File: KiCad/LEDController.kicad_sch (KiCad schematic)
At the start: 59 parts, among them J1 UART, J2 VDD, J3 GND, J4 Conn_01x05, J5 Conn_01x03, J6 USB_C_Receptacle_USB2.0_16P, J7 Conn_01x14, J8 JTAG, Q1 IRLZ44N, Q2 IRLZ44N, Q3 IRLZ44N, Q4 IRLZ44N, SW1 BOOT, SW2 EN, U1 TPS54202DDC, U2 ESP32-S3-WROOM-2, U3 TPS54202DDC

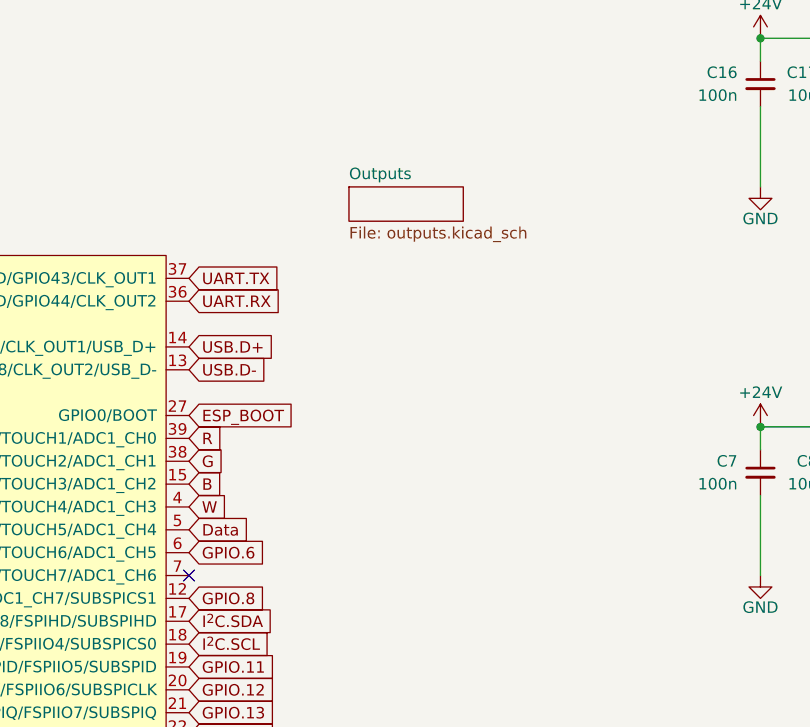
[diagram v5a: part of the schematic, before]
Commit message: add relay
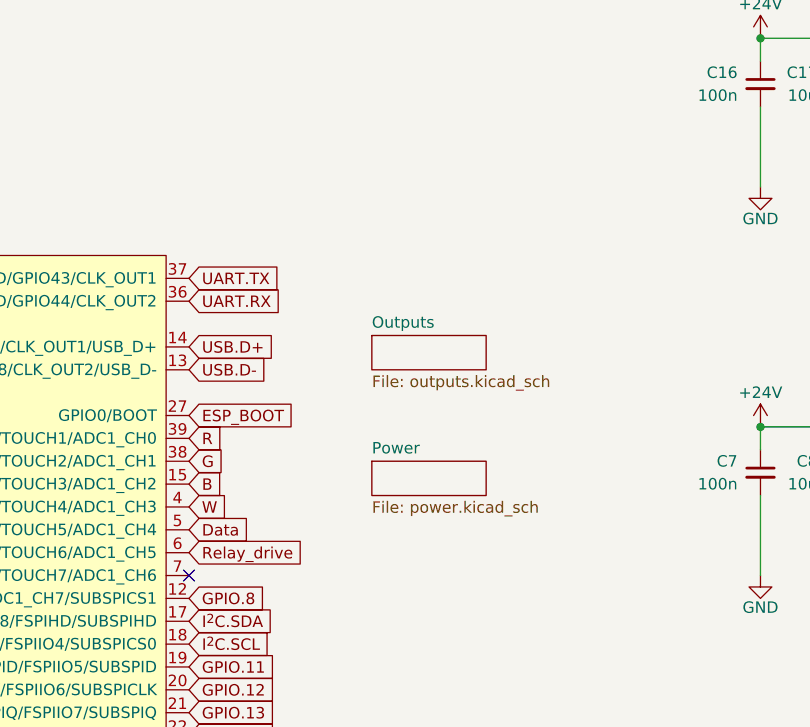
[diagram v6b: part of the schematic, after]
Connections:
- net GPIO.6: no longer U2.6 (GPIO6/TOUCH6/ADC1_CH5)
- new net Relay_drive: U2.6 (GPIO6/TOUCH6/ADC1_CH5)
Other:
- added sheet Power (power.kicad_sch)

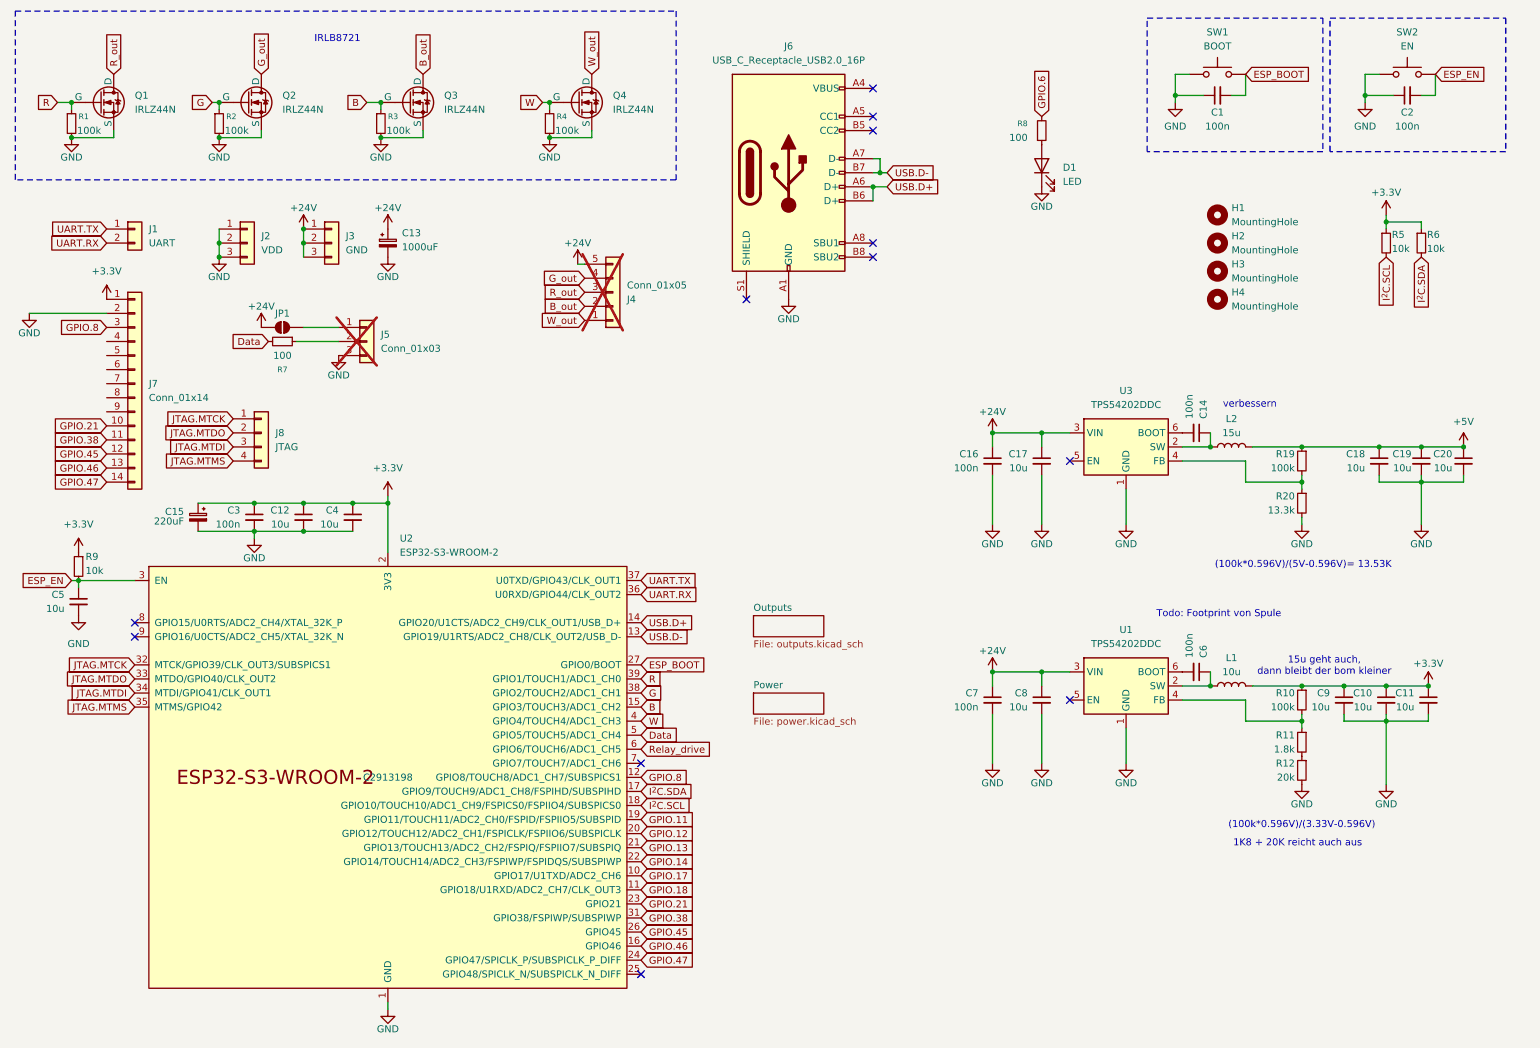
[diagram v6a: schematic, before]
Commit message: delete pwm, add 12 neopixel outputs
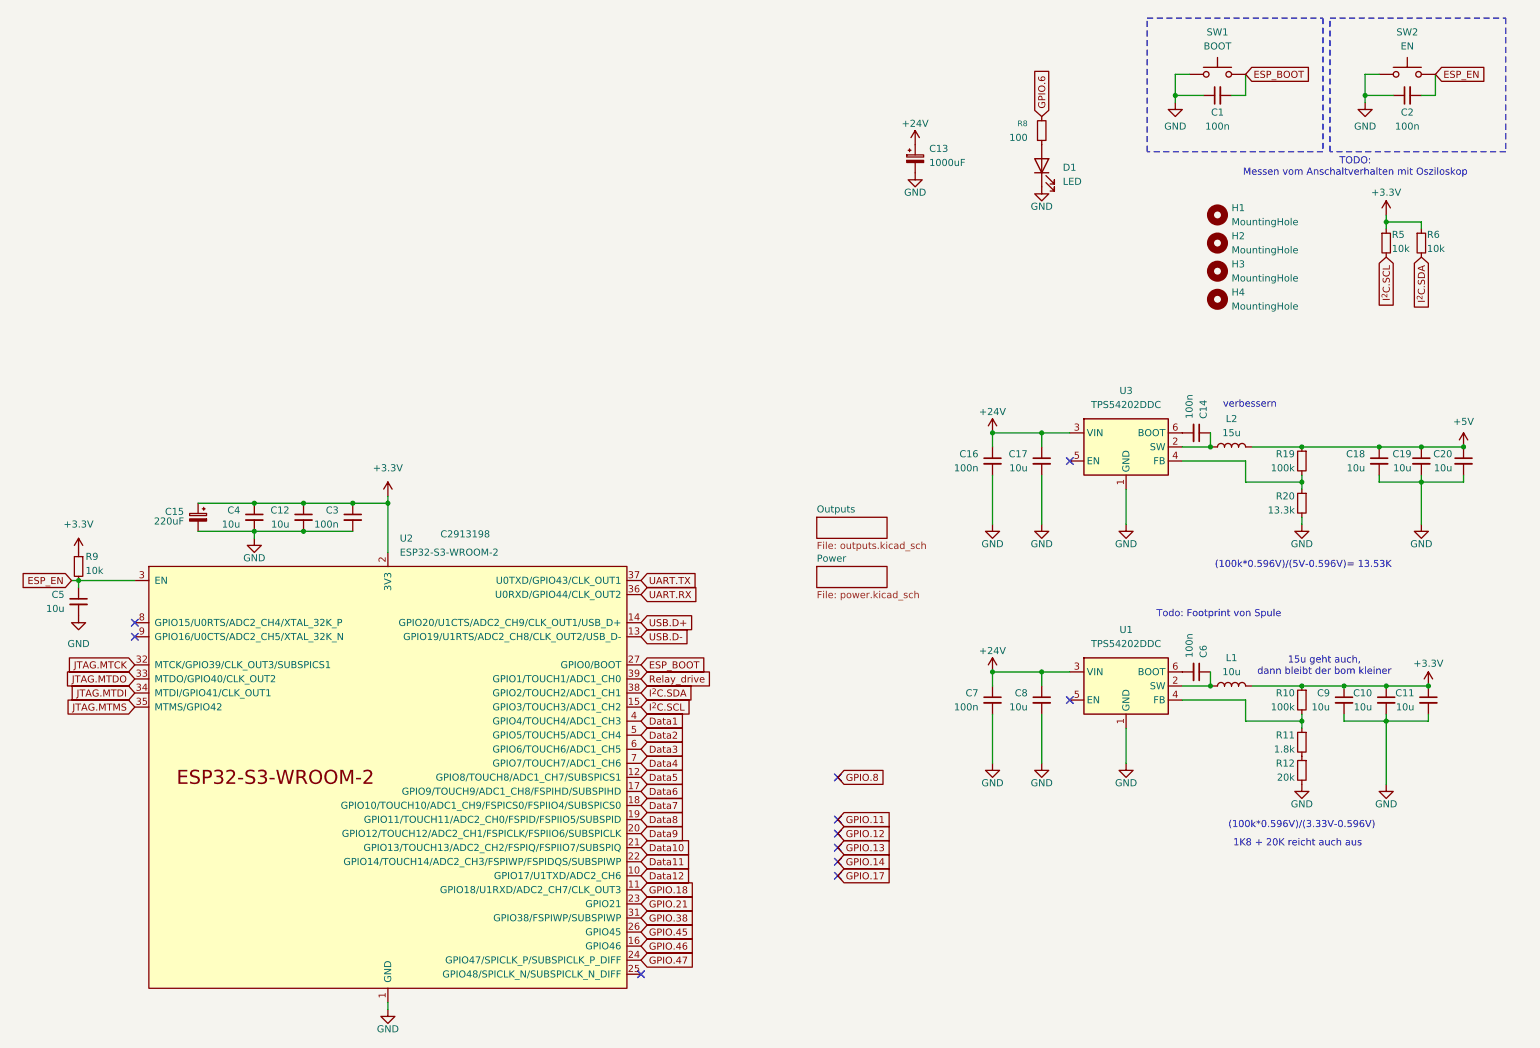
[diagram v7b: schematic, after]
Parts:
- removed J1: UART, Connector_PinHeader_2.54mm:PinHeader_1x02_P2.54mm_Vertical, symbol Connector_Generic:Conn_01x02
- removed J2: VDD, TerminalBlock_Phoenix:TerminalBlock_Phoenix_MKDS-1,5-3-5.08_1x03_P5.08mm_Horizontal, symbol Connector_Generic:Conn_01x03
- removed J3: GND, TerminalBlock_Phoenix:TerminalBlock_Phoenix_MKDS-1,5-3-5.08_1x03_P5.08mm_Horizontal, symbol Connector_Generic:Conn_01x03
- removed J4: Conn_01x05, Connector_JST:JST_XH_B5B-XH-A_1x05_P2.50mm_Vertical, symbol Connector_Generic:Conn_01x05
- removed J5: Conn_01x03, Connector_JST:JST_XH_B3B-XH-A_1x03_P2.50mm_Vertical, symbol Connector_Generic:Conn_01x03
- removed J6: USB_C_Receptacle_USB2.0_16P, Connector_USB:USB_C_Receptacle_GCT_USB4105-xx-A_16P_TopMnt_Horizontal, symbol Connector:USB_C_Receptacle_USB2.0_16P
- removed J7: Conn_01x14, Connector_PinHeader_2.54mm:PinHeader_1x14_P2.54mm_Vertical, symbol Connector_Generic:Conn_01x14
- removed J8: JTAG, Connector_PinHeader_2.54mm:PinHeader_1x04_P2.54mm_Vertical, symbol Connector_Generic:Conn_01x04
- removed JP1: SolderJumper_2_Open, Jumper:SolderJumper-2_P1.3mm_Open_RoundedPad1.0x1.5mm, symbol Jumper:SolderJumper_2_Open
- removed Q1, Q2, Q3, Q4: IRLZ44N, Package_TO_SOT_THT:TO-220-3_Vertical, symbol Simulation_SPICE:NMOS
- removed R1, R2, R3, R4: 100k, Resistor_SMD:R_0805_2012Metric_Pad1.20x1.40mm_HandSolder, symbol Device:R_Small
- removed R7: 100, Resistor_SMD:R_0805_2012Metric_Pad1.20x1.40mm_HandSolder, symbol Device:R_Small
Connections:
- net B is gone; now on net I^{2}C.SCL: U2.15 (GPIO3/TOUCH3/ADC1_CH2)
- net G is gone; now on net I^{2}C.SDA: U2.38 (GPIO2/TOUCH2/ADC1_CH1)
- net R is gone; now on net Relay_drive: U2.39 (GPIO1/TOUCH1/ADC1_CH0)
- net GPIO.11: no longer U2.19 (GPIO11/TOUCH11/ADC2_CH0/FSPID/FSPIIO5/SUBSPID)
- net GPIO.12: no longer U2.20 (GPIO12/TOUCH12/ADC2_CH1/FSPICLK/FSPIIO6/SUBSPICLK)
- net GPIO.13: no longer U2.21 (GPIO13/TOUCH13/ADC2_CH2/FSPIQ/FSPIIO7/SUBSPIQ)
- net GPIO.14: no longer U2.22 (GPIO14/TOUCH14/ADC2_CH3/FSPIWP/FSPIDQS/SUBSPIWP)
- net GPIO.17: no longer U2.10 (GPIO17/U1TXD/ADC2_CH6)
- net GPIO.8: no longer U2.12 (GPIO8/TOUCH8/ADC1_CH7/SUBSPICS1)
- net I^{2}C.SCL: no longer U2.18 (GPIO10/TOUCH10/ADC1_CH9/FSPICS0/FSPIIO4/SUBSPICS0)
- net I^{2}C.SDA: no longer U2.17 (GPIO9/TOUCH9/ADC1_CH8/FSPIHD/SUBSPIHD)
- net Relay_drive: no longer U2.6 (GPIO6/TOUCH6/ADC1_CH5)
- net Data4: now reaches U2.7 (GPIO7/TOUCH7/ADC1_CH6)
- net Data renamed Data2
- net W renamed Data1
- new net Data10: U2.21 (GPIO13/TOUCH13/ADC2_CH2/FSPIQ/FSPIIO7/SUBSPIQ)
- new net Data11: U2.22 (GPIO14/TOUCH14/ADC2_CH3/FSPIWP/FSPIDQS/SUBSPIWP)
- new net Data12: U2.10 (GPIO17/U1TXD/ADC2_CH6)
- new net Data3: U2.6 (GPIO6/TOUCH6/ADC1_CH5)
- new net Data5: U2.12 (GPIO8/TOUCH8/ADC1_CH7/SUBSPICS1)
- new net Data6: U2.17 (GPIO9/TOUCH9/ADC1_CH8/FSPIHD/SUBSPIHD)
- new net Data7: U2.18 (GPIO10/TOUCH10/ADC1_CH9/FSPICS0/FSPIIO4/SUBSPICS0)
- new net Data8: U2.19 (GPIO11/TOUCH11/ADC2_CH0/FSPID/FSPIIO5/SUBSPID)
- new net Data9: U2.20 (GPIO12/TOUCH12/ADC2_CH1/FSPICLK/FSPIIO6/SUBSPICLK)
- no-connect marks 12 -> 11
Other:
- note added: "TODO: Messen vom Anschaltverhalten mit Osziloskop"
- note removed: "IRLB8721"
- moved on the sheet: C13, C3, C4

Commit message: work on new design
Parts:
- added C21: 220uF, Capacitor_THT:CP_Radial_D8.0mm_P3.50mm, symbol Device:C_Polarized_Small
- L2: footprint Inductor_SMD:L_APV_ANR4026 -> Inductor_SMD:L_APV_APH0420
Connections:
- net +5V: now also C21.1
- net GND: now also C21.2
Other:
- moved on the sheet: C14, C16, C17, C18, C19, C20, L2, R19, R20, U3
